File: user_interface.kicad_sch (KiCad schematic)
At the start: 18 parts, among them Q2 IRLML6344T, SW3 SW_Push, SW4 SW_Push, SW5 SW_Push

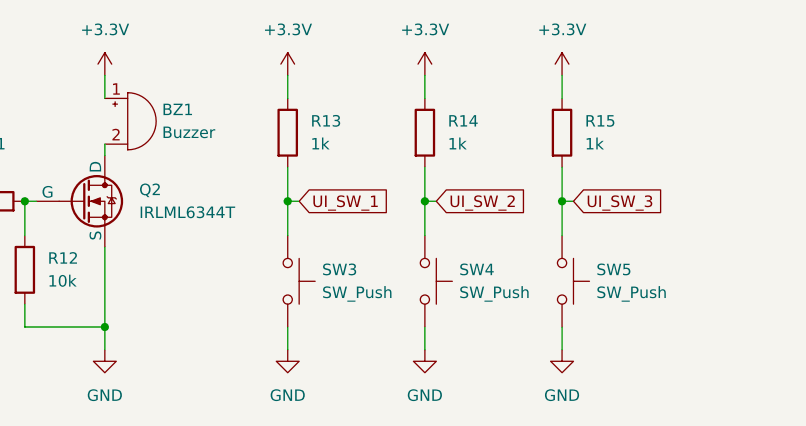
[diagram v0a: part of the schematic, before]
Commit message: UIのブザー型番を追記
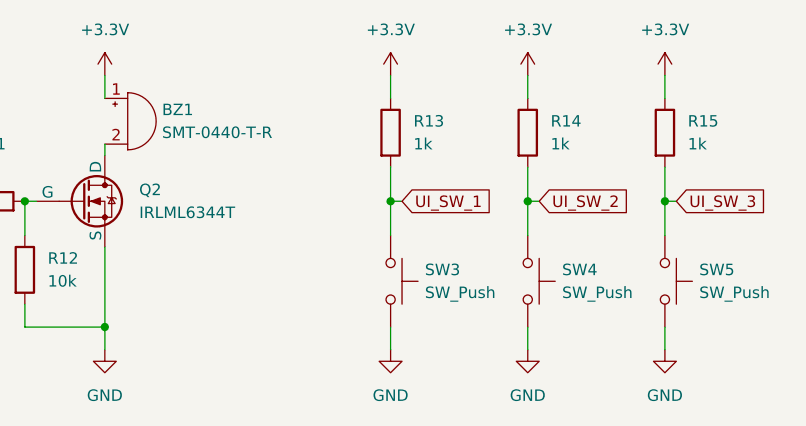
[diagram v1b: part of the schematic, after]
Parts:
- BZ1: value Buzzer -> SMT-0440-T-R
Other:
- moved on the sheet: R13, R14, R15, SW3, SW4, SW5

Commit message: アノテーション番号ミスの修正とフットプリント割り当て途中（部品リストも途中生成）
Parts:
- D3, D4, D5, D6: footprint (none) -> LED_SMD:LED_0603_1608Metric_Pad1.05x0.95mm_HandSolder
- Q2: footprint (none) -> Package_TO_SOT_SMD:SOT-23
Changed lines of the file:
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@@
       (effects (font (size 1.27 1.27)) (justify left))
     )
-    (property "Footprint" "" (at 175.26 90.17 0)
+    (property "Footprint" "Package_TO_SOT_SMD:SOT-23" (at 175.26 90.17 0)
       (effects (font (size 1.27 1.27)) hide)
     )
@@
       (effects (font (size 1.27 1.27)) (justify right))
     )
-    (property "Footprint" "" (at 97.79 101.6 0)
+    (property "Footprint" "LED_SMD:LED_0603_1608Metric_Pad1.05x0.95mm_HandSolder" (at 97.79 101.6 0)
       (effects (font (size 1.27 1.27)) hide)
     )
@@
       (effects (font (size 1.27 1.27)) (justify right))
     )
-    (property "Footprint" "" (at 60.96 101.6 0)
+    (property "Footprint" "LED_SMD:LED_0603_1608Metric_Pad1.05x0.95mm_HandSolder" (at 60.96 101.6 0)
       (effects (font (size 1.27 1.27)) hide)
     )
@@
       (effects (font (size 1.27 1.27)) (justify right))
     )
-    (property "Footprint" "" (at 80.01 101.6 0)
+    (property "Footprint" "LED_SMD:LED_0603_1608Metric_Pad1.05x0.95mm_HandSolder" (at 80.01 101.6 0)
       (effects (font (size 1.27 1.27)) hide)
     )
@@
       (effects (font (size 1.27 1.27)) (justify right))
     )
-    (property "Footprint" "" (at 115.57 101.6 0)
-      (effects (font (size 1.27 1.27)) hide)
-    )
+    (property "Footprint" "LED_SMD:LED_0603_1608Metric_Pad1.05x0.95mm_HandSolder" (at 115.57 101.6 0)
+      (effects (font (size 1.27 1.27)) hide)
+    )

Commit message: フェライトビーズに型番追加し、自作パッケージの構成へこう
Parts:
- R10, R11, R12, R13, R14, R15, R7, R8, R9: footprint (none) -> Resistor_SMD:R_0603_1608Metric_Pad0.98x0.95mm_HandSolder
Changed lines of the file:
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@@
       (effects (font (size 1.27 1.27)) (justify left))
     )
-    (property "Footprint" "" (at 202.692 85.09 90)
+    (property "Footprint" "Resistor_SMD:R_0603_1608Metric_Pad0.98x0.95mm_HandSolder" (at 202.692 85.09 90)
       (effects (font (size 1.27 1.27)) hide)
     )
@@
       (effects (font (size 1.27 1.27)) (justify left))
     )
-    (property "Footprint" "" (at 59.182 93.98 90)
+    (property "Footprint" "Resistor_SMD:R_0603_1608Metric_Pad0.98x0.95mm_HandSolder" (at 59.182 93.98 90)
       (effects (font (size 1.27 1.27)) hide)
     )
@@
       (effects (font (size 1.27 1.27)) (justify left))
     )
-    (property "Footprint" "" (at 233.172 85.09 90)
+    (property "Footprint" "Resistor_SMD:R_0603_1608Metric_Pad0.98x0.95mm_HandSolder" (at 233.172 85.09 90)
       (effects (font (size 1.27 1.27)) hide)
     )
@@
       (effects (font (size 1.27 1.27)))
     )
-    (property "Footprint" "" (at 160.02 94.488 90)
+    (property "Footprint" "Resistor_SMD:R_0603_1608Metric_Pad0.98x0.95mm_HandSolder" (at 160.02 94.488 90)
       (effects (font (size 1.27 1.27)) hide)
     )
@@
       (effects (font (size 1.27 1.27)) (justify left))
     )
-    (property "Footprint" "" (at 162.052 100.33 90)
+    (property "Footprint" "Resistor_SMD:R_0603_1608Metric_Pad0.98x0.95mm_HandSolder" (at 162.052 100.33 90)
       (effects (font (size 1.27 1.27)) hide)
     )
@@
       (effects (font (size 1.27 1.27)) (justify left))
     )
-    (property "Footprint" "" (at 96.012 93.98 90)
+    (property "Footprint" "Resistor_SMD:R_0603_1608Metric_Pad0.98x0.95mm_HandSolder" (at 96.012 93.98 90)
       (effects (font (size 1.27 1.27)) hide)
     )
@@
       (effects (font (size 1.27 1.27)) (justify left))
     )
-    (property "Footprint" "" (at 217.932 85.09 90)
+    (property "Footprint" "Resistor_SMD:R_0603_1608Metric_Pad0.98x0.95mm_HandSolder" (at 217.932 85.09 90)
       (effects (font (size 1.27 1.27)) hide)
     )
@@
       (effects (font (size 1.27 1.27)) (justify left))
     )
-    (property "Footprint" "" (at 113.792 93.98 90)
+    (property "Footprint" "Resistor_SMD:R_0603_1608Metric_Pad0.98x0.95mm_HandSolder" (at 113.792 93.98 90)
       (effects (font (size 1.27 1.27)) hide)
     )
@@
       (effects (font (size 1.27 1.27)) (justify left))
     )
-    (property "Footprint" "" (at 78.232 93.98 90)
-      (effects (font (size 1.27 1.27)) hide)
-    )
+    (property "Footprint" "Resistor_SMD:R_0603_1608Metric_Pad0.98x0.95mm_HandSolder" (at 78.232 93.98 90)
+      (effects (font (size 1.27 1.27)) hide)
+    )

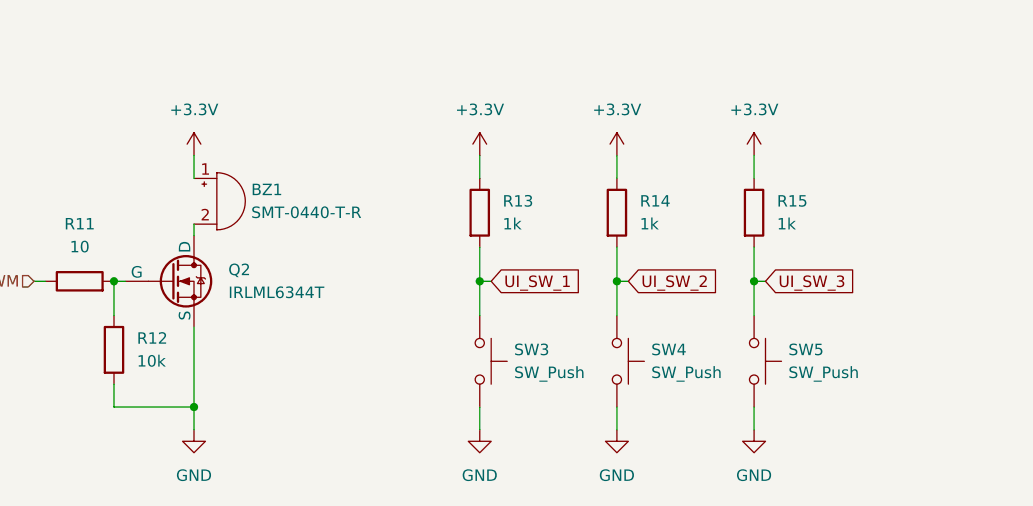
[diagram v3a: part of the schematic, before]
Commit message: ブザーSMT-0440のフットプリントとシンボルをインポートして、回路図のシンボルを変更した。
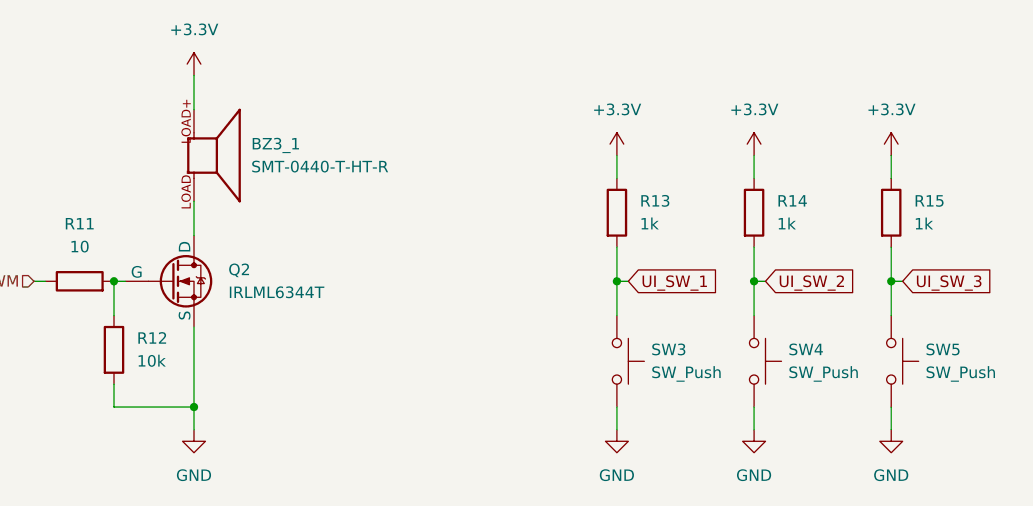
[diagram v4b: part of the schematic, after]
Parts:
- removed BZ1: SMT-0440-T-R, symbol Device:Buzzer
- added BZ3_1: SMT-0440-T-HT-R, SMT-0440-T-HT-R:XDCR_SMT-0440-T-HT-R, symbol SMT-0440-T-HT-R:SMT-0440-T-HT-R
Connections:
- net +3.3V: now also BZ3_1.LOAD+
- net at Q2.1 (D): now also BZ3_1.LOAD-
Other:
- moved on the sheet: R13, R14, R15, SW3, SW4, SW5

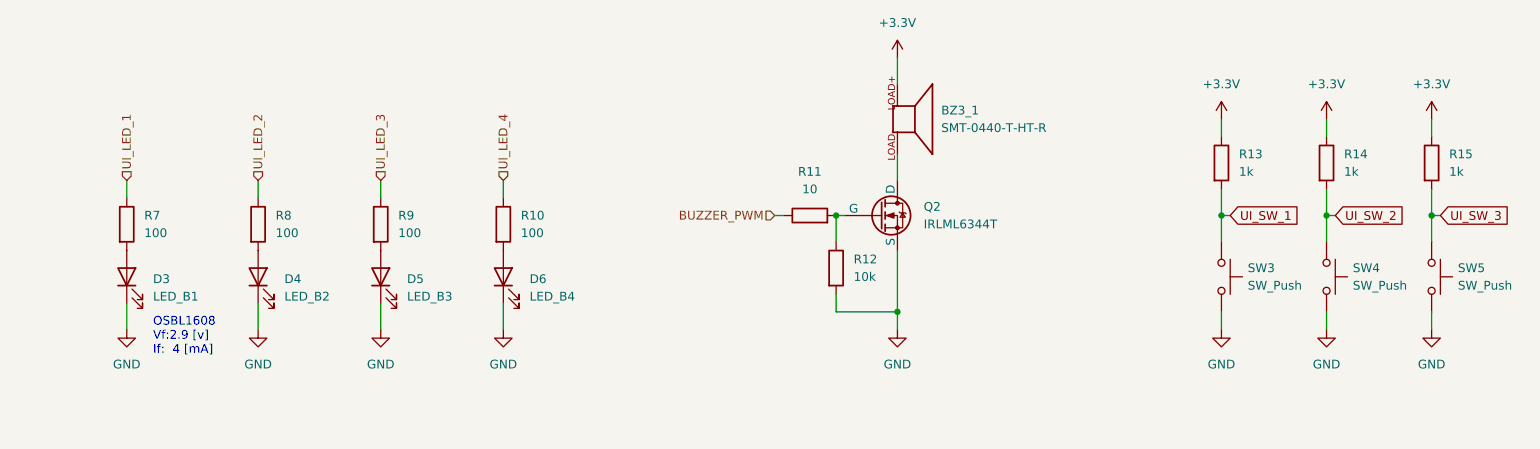
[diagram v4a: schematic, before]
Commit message: スイッチ以外のフットプリント割当完了
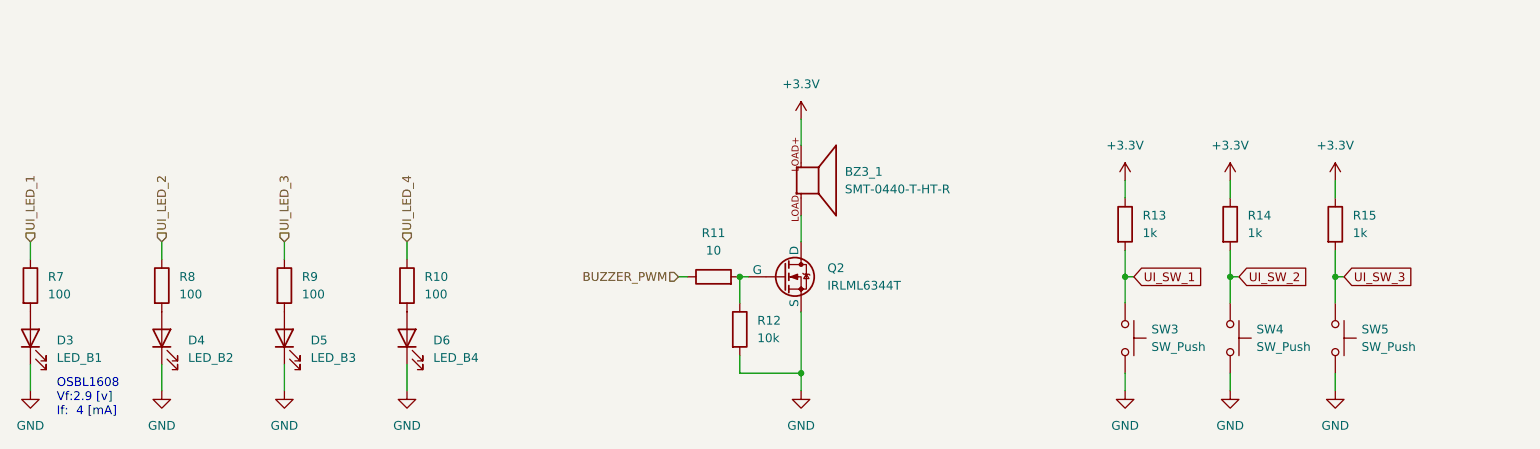
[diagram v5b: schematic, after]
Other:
- moved on the sheet: BZ3_1, D3, D4, D5, D6, Q2, R10, R11, R12, R13, R14, R15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

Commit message: 秋月電子のスライドスイッチのフットプリントを追加して全てのフットプリント割当も完了
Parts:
- SW3, SW4, SW5: footprint (none) -> Button_Switch_THT:SW_PUSH_6mm
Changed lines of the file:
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@@
       (effects (font (size 1.27 1.27)) (justify left))
     )
-    (property "Footprint" "" (at 241.3 110.49 0)
+    (property "Footprint" "Button_Switch_THT:SW_PUSH_6mm" (at 241.3 110.49 0)
       (effects (font (size 1.27 1.27)) hide)
     )
@@
       (effects (font (size 1.27 1.27)) (justify left))
     )
-    (property "Footprint" "" (at 226.06 110.49 0)
+    (property "Footprint" "Button_Switch_THT:SW_PUSH_6mm" (at 226.06 110.49 0)
       (effects (font (size 1.27 1.27)) hide)
     )
@@
       (effects (font (size 1.27 1.27)) (justify left))
     )
-    (property "Footprint" "" (at 210.82 110.49 0)
-      (effects (font (size 1.27 1.27)) hide)
-    )
+    (property "Footprint" "Button_Switch_THT:SW_PUSH_6mm" (at 210.82 110.49 0)
+      (effects (font (size 1.27 1.27)) hide)
+    )

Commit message: 押しボタンスイッチのフットプリント割り当てを変更
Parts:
- SW3, SW4, SW5: footprint Button_Switch_THT:SW_PUSH_6mm -> Button_Switch_THT:SW_PUSH_1P1T_6x3.5mm_H4.3_APEM_MJTP1243
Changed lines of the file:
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@@
       (effects (font (size 1.27 1.27)) (justify left))
     )
-    (property "Footprint" "Button_Switch_THT:SW_PUSH_6mm" (at 241.3 110.49 0)
+    (property "Footprint" "Button_Switch_THT:SW_PUSH_1P1T_6x3.5mm_H4.3_APEM_MJTP1243" (at 241.3 110.49 0)
       (effects (font (size 1.27 1.27)) hide)
     )
@@
       (effects (font (size 1.27 1.27)) (justify left))
     )
-    (property "Footprint" "Button_Switch_THT:SW_PUSH_6mm" (at 226.06 110.49 0)
+    (property "Footprint" "Button_Switch_THT:SW_PUSH_1P1T_6x3.5mm_H4.3_APEM_MJTP1243" (at 226.06 110.49 0)
       (effects (font (size 1.27 1.27)) hide)
     )
@@
       (effects (font (size 1.27 1.27)) (justify left))
     )
-    (property "Footprint" "Button_Switch_THT:SW_PUSH_6mm" (at 210.82 110.49 0)
-      (effects (font (size 1.27 1.27)) hide)
-    )
+    (property "Footprint" "Button_Switch_THT:SW_PUSH_1P1T_6x3.5mm_H4.3_APEM_MJTP1243" (at 210.82 110.49 0)
+      (effects (font (size 1.27 1.27)) hide)
+    )

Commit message: UIスイッチ３種類をマイコンピンに割り当て忘れてたので割り当てた
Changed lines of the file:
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@@
     (effects (font (size 1.27 1.27)) (justify left bottom))
   )
-  (global_label "UI_SW_3" (shape input) (at 237.49 101.6 0) (fields_autoplaced)
+  (hierarchical_label "UI_SW_1" (shape output) (at 207.01 101.6 0) (fields_autoplaced)
     (effects (font (size 1.27 1.27)) (justify left))
-    (property "Intersheetrefs" "${INTERSHEET_REFS}" (at 248.2161 101.6 0)
-      (effects (font (size 1.27 1.27)) (justify left) hide)
-    )
-  )
-  (global_label "UI_SW_2" (shape input) (at 222.25 101.6 0) (fields_autoplaced)
-    (effects (font (size 1.27 1.27)) (justify left))
-    (property "Intersheetrefs" "${INTERSHEET_REFS}" (at 232.9761 101.6 0)
-      (effects (font (size 1.27 1.27)) (justify left) hide)
-    )
-  )
-  (global_label "UI_SW_1" (shape input) (at 207.01 101.6 0) (fields_autoplaced)
-    (effects (font (size 1.27 1.27)) (justify left))
-    (property "Intersheetrefs" "${INTERSHEET_REFS}" (at 217.7361 101.6 0)
-      (effects (font (size 1.27 1.27)) (justify left) hide)
-    )
   )
   (hierarchical_label "BUZZER_PWM" (shape input) (at 140.97 101.6 180) (fields_autoplaced)
@@
     (effects (font (size 1.27 1.27)) (justify left))
   )
+  (hierarchical_label "UI_SW_3" (shape output) (at 237.49 101.6 0) (fields_autoplaced)
+    (effects (font (size 1.27 1.27)) (justify left))
+  )
+  (hierarchical_label "UI_SW_2" (shape output) (at 222.25 101.6 0) (fields_autoplaced)
+    (effects (font (size 1.27 1.27)) (justify left))
+  )
